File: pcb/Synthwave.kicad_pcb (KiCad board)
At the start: 2 copper layers, 68.8 x 136.6 mm, 62 parts, among them J1 Conn_01x01_Pin, J2 Conn_01x01_Pin, P1 MINI-360, P2 MINI-360, Q1 TIP120, Q10 TIP120, Q2 TIP120, Q3 TIP120, Q4 TIP120, Q5 TIP120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

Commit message: Many small updates
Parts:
- added J3: ADC1, Connector_PinSocket_2.54mm:PinSocket_1x03_P2.54mm_Vertical, F.Cu at (66.0, 16.5)
- added J4: ADC2, Connector_PinSocket_2.54mm:PinSocket_1x03_P2.54mm_Vertical, F.Cu at (67.0, 45.7)
- added J5: ADC3, Connector_PinSocket_2.54mm:PinSocket_1x03_P2.54mm_Vertical, F.Cu at (71.6, 45.7)
- added J6: ADC4, Connector_PinSocket_2.54mm:PinSocket_1x03_P2.54mm_Vertical, F.Cu at (76.2, 45.7)
- U1: value Heltec_HTIT-WB32 -> Heltec_HTIT-WB32v3
- moved U2 8.84 mm to (52.1, 52.4)
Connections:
- P2 pad 2: Net-(P2-OUT-) -> Net-(J3-PIN_3)
- P2 pad 3: Net-(P2-OUT+) -> Net-(J3-Pin_2)
- R1 pad 2: Net-(R1-Pad2) -> Net-(U1-7_ADC)
- R10 pad 2: Net-(R10-Pad2) -> Net-(U1-42)
- R11 pad 1: Net-(R1-Pad2) -> Net-(U1-7_ADC)
- R12 pad 1: Net-(R12-Pad1) -> Net-(U1-6_ADC)
- R13 pad 1: Net-(U1-25_DAC) -> Net-(U1-33)
- R14 pad 1: Net-(R14-Pad1) -> Net-(U1-47)
- R15 pad 1: Net-(R15-Pad1) -> Net-(U1-48)
- R16 pad 1: Net-(R16-Pad1) -> Net-(U1-46)
- R17 pad 1: Net-(R17-Pad1) -> Net-(U1-5_ADC)
- R18 pad 1: Net-(R18-Pad1) -> Net-(U1-34)
- R19 pad 1: Net-(R19-Pad1) -> Net-(U1-45)
- R2 pad 2: Net-(R12-Pad1) -> Net-(U1-6_ADC)
- R20 pad 1: Net-(R10-Pad2) -> Net-(U1-42)
- R3 pad 2: Net-(U1-25_DAC) -> Net-(U1-33)
- R4 pad 2: Net-(R14-Pad1) -> Net-(U1-47)
- R5 pad 2: Net-(R15-Pad1) -> Net-(U1-48)
- R6 pad 2: Net-(R16-Pad1) -> Net-(U1-46)
- R7 pad 2: Net-(R17-Pad1) -> Net-(U1-5_ADC)
- R8 pad 2: Net-(R18-Pad1) -> Net-(U1-34)
- R9 pad 2: Net-(R19-Pad1) -> Net-(U1-45)
- U1 pad 1: unconnected-(U1-TX-Pad1) -> Net-(U1-48)
- U1 pad 12: Net-(R18-Pad1) -> unconnected-(U1-43_TX-Pad12)
- U1 pad 13: Net-(R17-Pad1) -> unconnected-(U1-44_RX-Pad13)
- U1 pad 14: Net-(R1-Pad2) -> unconnected-(U1-RST-Pad14)
- U1 pad 15: unconnected-(U1-15_OLED-Pad15) -> Net-(U1-33)
- U1 pad 17: Net-(R16-Pad1) -> unconnected-(U1-38-Pad17)
- U1 pad 18: unconnected-(U1-Pad18) -> Net-(U1-40)
- U1 pad 19: unconnected-(U1-Pad19) -> Net-(U1-42)
- U1 pad 2: Net-(R19-Pad1) -> Net-(U1-34)
- U1 pad 20: Net-(P2-OUT+) -> unconnected-(U1-3.3V-Pad20)
- U1 pad 21: unconnected-(U1-Pad21) -> Net-(U1-46)
- U1 pad 22: unconnected-(U1-Pad22) -> Net-(U1-45)
- U1 pad 23: Net-(R10-Pad2) -> Net-(U1-41)
- U1 pad 25: Net-(U1-25_DAC) -> unconnected-(U1-20-Pad25)
- U1 pad 27: Net-(R12-Pad1) -> unconnected-(U1-USER_SW_0-Pad27)
- U1 pad 28: Net-(P2-OUT-) -> unconnected-(U1-GND-Pad28)
- U1 pad 3: unconnected-(U1-RX-Pad3) -> Net-(U1-47)
- U1 pad 32: Net-(R15-Pad1) -> Net-(U1-7_ADC)
- U1 pad 33: Net-(R14-Pad1) -> unconnected-(U1-19_CLK-Pad33)
- U1 pad 34: Net-(U2-IB) -> Net-(U1-5_ADC)
- U1 pad 35: Net-(U2-IA) -> Net-(U1-6_ADC)
- U1 pad 36: unconnected-(U1-Pad36) -> Net-(J3-Pin_1)
- U1 pad 37: unconnected-(U1-Pad37) -> Net-(J4-Pin_1)
- U1 pad 38: unconnected-(U1-Pad38) -> Net-(J5-Pin_1)
- U1 pad 39: unconnected-(U1-Pad39) -> Net-(J6-Pin_1)
- U1 pad 8: unconnected-(U1-GND-Pad8) -> Net-(J3-PIN_3)
- U1 pad 9: unconnected-(U1-3.3-Pad9) -> Net-(J3-Pin_2)
- U2 pad 5: Net-(P2-OUT-) -> Net-(J3-PIN_3)
- U2 pad 6: Net-(U2-IA) -> Net-(U1-40)
- U2 pad 7: Net-(U2-IB) -> Net-(U1-41)
- U2 pad 8: Net-(P2-OUT-) -> Net-(J3-PIN_3)
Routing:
- net GND: track 300.9 -> 0.00 mm
- net +15V: track 266.4 -> 0.00 mm
- net Net-(R1-Pad2): track 112.5 -> 0.00 mm
- net Net-(P2-OUT-): track 93.5 -> 0.00 mm
- net Net-(R12-Pad1): track 91.5 -> 0.00 mm, vias 1 -> 0
- net Net-(U1-25_DAC): track 89.5 -> 0.00 mm
- net Net-(R14-Pad1): track 81.5 -> 0.00 mm
- net Net-(P2-OUT+): track 68.1 -> 0.00 mm
- net Net-(R10-Pad2): track 67.1 -> 0.00 mm
- net Net-(R17-Pad1): track 63.9 -> 0.00 mm
- net Net-(U2-IB): track 54.5 -> 0.00 mm
- net Net-(U2-IA): track 53.3 -> 0.00 mm
- net Net-(R18-Pad1): track 52.3 -> 0.00 mm
- net Net-(R15-Pad1): track 48.8 -> 0.00 mm
- net Net-(E2-Pin_1): track 42.0 -> 0.00 mm
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
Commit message: Update and upgrades
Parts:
- removed DC_OUT1, DC_OUT10, DC_OUT2, DC_OUT3, DC_OUT4, DC_OUT5, DC_OUT6, DC_OUT7, DC_OUT8, DC_OUT9: GND, Connector_PinSocket_2.54mm:PinSocket_1x02_P2.54mm_Vertical
- removed the G*** at (65.1, 136.6)
- added G***: LOGO, Untitled, F.Cu at (58.4, 118.1)
- added J7: RX, Connector_PinSocket_2.54mm:PinSocket_1x02_P2.54mm_Vertical, F.Cu at (67.3, 58.4)
- added J8: RX, Connector_PinSocket_2.54mm:PinSocket_1x02_P2.54mm_Vertical, F.Cu at (71.1, 58.4)
- added PUMP1: GND, Connector_PinSocket_2.54mm:PinSocket_1x02_P2.54mm_Vertical, F.Cu at (20.3, 26.7)
- added PUMP2: GND, Connector_PinSocket_2.54mm:PinSocket_1x02_P2.54mm_Vertical, F.Cu at (20.3, 35.6)
- added REL1: GND, Connector_PinSocket_2.54mm:PinSocket_1x02_P2.54mm_Vertical, F.Cu at (20.3, 102.9)
- added REL2: GND, Connector_PinSocket_2.54mm:PinSocket_1x02_P2.54mm_Vertical, F.Cu at (20.3, 110.5)
- added VAC1: GND, Connector_PinSocket_2.54mm:PinSocket_1x02_P2.54mm_Vertical, F.Cu at (20.3, 83.8)
- added VAC2: GND, Connector_PinSocket_2.54mm:PinSocket_1x02_P2.54mm_Vertical, F.Cu at (20.3, 94.0)
- added VALVE1: GND, Connector_PinSocket_2.54mm:PinSocket_1x02_P2.54mm_Vertical, F.Cu at (20.3, 44.5)
- added VALVE2: GND, Connector_PinSocket_2.54mm:PinSocket_1x02_P2.54mm_Vertical, F.Cu at (20.3, 53.3)
- added VALVE3: GND, Connector_PinSocket_2.54mm:PinSocket_1x02_P2.54mm_Vertical, F.Cu at (20.3, 62.2)
- added VALVE4: GND, Connector_PinSocket_2.54mm:PinSocket_1x02_P2.54mm_Vertical, F.Cu at (20.3, 72.4)
- moved H3 28.1 mm to (71.1, 119.4)
- moved H2 27.1 mm to (19.1, 119.4)
- moved D10 26.1 mm to (24.1, 119.6)
- moved R10 25.2 mm to (36.9, 114.3)
- moved R20 25.2 mm to (36.9, 119.4)
- moved Q10 25.2 mm to (26.6, 115.5)
- moved U2 22.2 mm to (55.9, 30.5)
- moved D9 22.1 mm to (24.0, 109.5)
- moved R19 20.9 mm to (36.8, 109.5)
- moved R9 20.9 mm to (36.8, 104.4)
- moved Q9 20.9 mm to (26.5, 105.5)
- moved J3 19.1 mm to (67.3, 35.6)
- moved D8 18.5 mm to (24.0, 99.3)
- moved R8 17.4 mm to (36.8, 94.2)
- moved R18 17.4 mm to (36.8, 99.3)
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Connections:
- U1 pad 12: unconnected-(U1-43_TX-Pad12) -> Net-(J7-Pin_1)
- U1 pad 13: unconnected-(U1-44_RX-Pad13) -> Net-(J7-Pin_2)
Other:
- board size 68.8 x 136.6 mm -> 57.1 x 102.9 mm

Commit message: updates
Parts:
- removed J2: Conn_01x01_Pin, Connector_PinSocket_2.54mm:PinSocket_1x01_P2.54mm_Vertical
- removed P2: MINI-360, Custom Footprints:MINI-360
- added J10: GPIO39, Connector_PinSocket_2.54mm:PinSocket_1x02_P2.54mm_Vertical, F.Cu at (61.0, 54.6)
- added J9: GPIO26, Connector_PinSocket_2.54mm:PinSocket_1x02_P2.54mm_Vertical, F.Cu at (56.9, 54.6)
- added NT1: NetTie_2, NetTie:NetTie-2_THT_Pad1.0mm, F.Cu at (62.7, 34.3)
- added U3: L7805, Package_TO_SOT_THT:TO-220-3_Vertical, F.Cu at (52.1, 58.4)
- J1: value Conn_01x01_Pin -> Barrel_Jack_Switch; footprint Connector_PinSocket_2.54mm:PinSocket_1x01_P2.54mm_Vertical -> Connector_BarrelJack:BarrelJack_Horizontal
- J7: value RX -> TX
- moved U2 10.9 mm to (66.8, 29.7), turned to 180 degrees
- moved J1 6.96 mm to (52.6, 32.9), turned to -90 degrees
- moved P1 2.54 mm to (55.9, 41.8)
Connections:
- net Net-(J3-Pin_2) renamed +5V
- J3 pad 3: Net-(J3-PIN_3) -> GND1
- J4 pad 3: Net-(J3-PIN_3) -> GND1
- J5 pad 3: Net-(J3-PIN_3) -> GND1
- J6 pad 3: Net-(J3-PIN_3) -> GND1
- J8 pad 1: Net-(J3-PIN_3) -> GND1
- R11 pad 2: GND -> GND1
- R12 pad 2: GND -> GND1
- R13 pad 2: GND -> GND1
- R14 pad 2: GND -> GND1
- R15 pad 2: GND -> GND1
- R16 pad 2: GND -> GND1
- R17 pad 2: GND -> GND1
- R18 pad 2: GND -> GND1
- R19 pad 2: GND -> GND1
- R20 pad 2: GND -> GND1
- U1 pad 10: unconnected-(U1-26-Pad10) -> Net-(J9-Pin_1)
- U1 pad 5: unconnected-(U1-39-Pad5) -> Net-(J10-Pin_1)
- U1 pad 8: Net-(J3-PIN_3) -> GND1
- U2 pad 5: Net-(J3-PIN_3) -> GND
- U2 pad 8: Net-(J3-PIN_3) -> GND
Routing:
- net +15V: track 0.00 -> 218.0 mm
- net GND1: track 0.00 -> 200.9 mm
- net GND: track 0.00 -> 146.8 mm
- net +5V: track 0.00 -> 128.7 mm
- net Net-(U1-7_ADC): track 0.00 -> 77.7 mm
- net Net-(U1-40): track 0.00 -> 75.2 mm
- net Net-(U1-6_ADC): track 0.00 -> 68.2 mm, vias 0 -> 1
- net Net-(U1-5_ADC): track 0.00 -> 63.2 mm, vias 0 -> 2
- net Net-(U1-33): track 0.00 -> 61.2 mm
- net Net-(U1-48): track 0.00 -> 55.6 mm
- net Net-(U1-47): track 0.00 -> 53.8 mm
- net Net-(U1-42): track 0.00 -> 53.2 mm
- net Net-(U1-41): track 0.00 -> 52.3 mm
- net Net-(J9-Pin_1): track 0.00 -> 51.8 mm, vias 0 -> 1
- net Net-(U1-45): track 0.00 -> 45.8 mm
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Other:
- board text added: "RX"
- board text added: "TX"

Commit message: Add model updates and various files
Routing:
- net Net-(U1-5_ADC): track 63.2 -> 115.2 mm, vias 2 -> 0
- net +15V: track 218.0 -> 191.9 mm
- net Net-(U1-7_ADC): track 77.7 -> 96.6 mm
- net Net-(U1-40): track 75.2 -> 57.4 mm
- net +5V: track 128.7 -> 115.7 mm
- net Net-(D9-A): track 32.8 -> 21.5 mm
- net Net-(U1-48): track 55.6 -> 46.2 mm
- net Net-(U1-45): track 45.8 -> 55.1 mm
- net Net-(U1-41): track 52.3 -> 61.6 mm
- net Net-(Q6-B): track 11.1 -> 19.4 mm
- net Net-(Q9-B): track 11.1 -> 19.4 mm
- net Net-(U1-34): track 16.9 -> 24.6 mm
- net GND1: track 200.9 -> 206.0 mm
- net Net-(D6-A): track 25.5 -> 21.7 mm
- net GND: track 146.8 -> 143.5 mm
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
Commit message: Update electrode information, many small tweaks
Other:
- board text removed: "RX"
- board text removed: "TX"
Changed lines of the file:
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@@
         (effects (font (size 1 1) (thickness 0.15)))
     )
-    (fp_text value "RX" (at 0 5.31) (layer "F.Fab")
+    (fp_text value "RX" (at 0 5.31) (layer "F.Fab") hide
         (effects (font (size 1 1) (thickness 0.15)))
     )
@@
         (effects (font (size 1 1) (thickness 0.15)))
     )
-    (fp_text value "TX" (at 0 5.31) (layer "F.Fab")
+    (fp_text value "TX" (at 0 5.31) (layer "F.Fab") hide
         (effects (font (size 1 1) (thickness 0.15)))
     )
@@
     (effects (font (size 1 1) (thickness 0.15)))
   )
-  (gr_text "RX" (at 70.104 64.262) (layer "F.SilkS")
-    (effects (font (size 1 1) (thickness 0.15)) (justify left bottom))
-  )
-  (gr_text "TX" (at 66.294 64.262) (layer "F.SilkS")
-    (effects (font (size 1 1) (thickness 0.15)) (justify left bottom))
-  )
   (gr_text "GND" (at 52.578 24.384) (layer "F.SilkS")

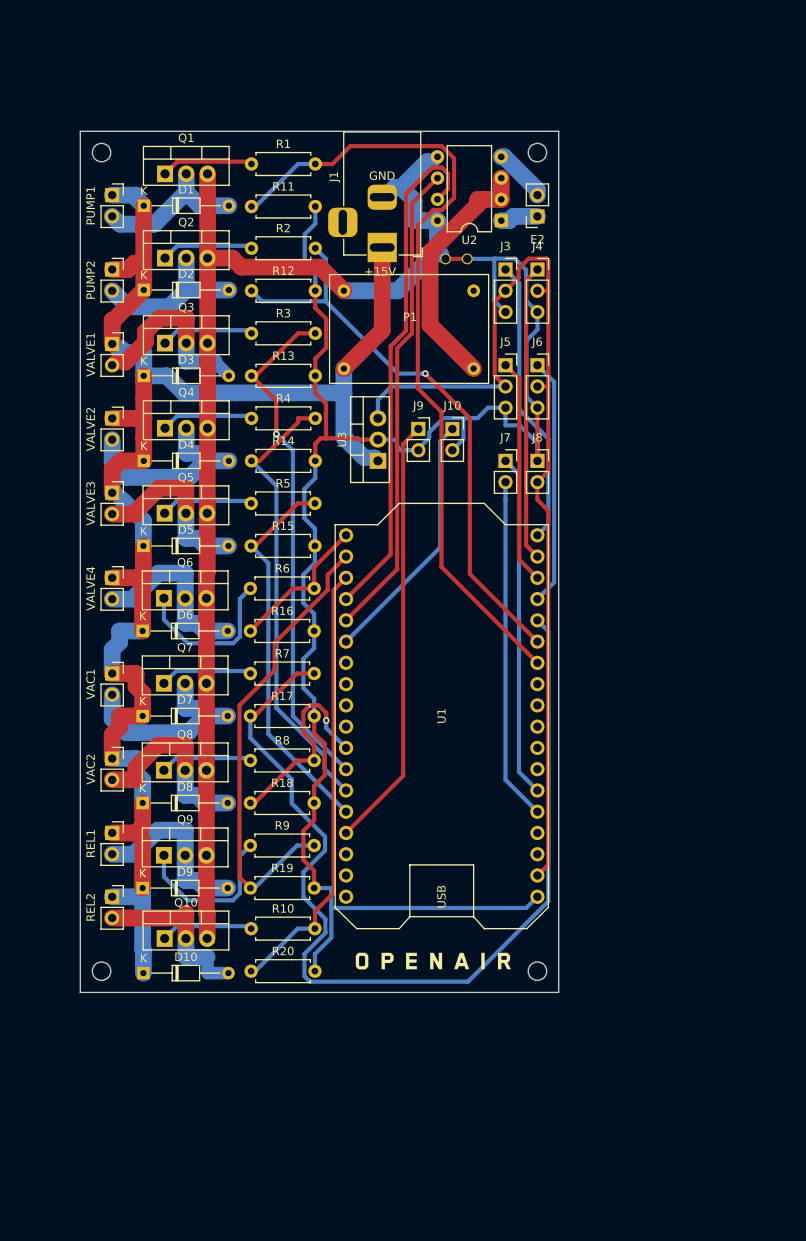
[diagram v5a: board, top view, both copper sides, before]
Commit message: Add lots and lots of connectors to PCB
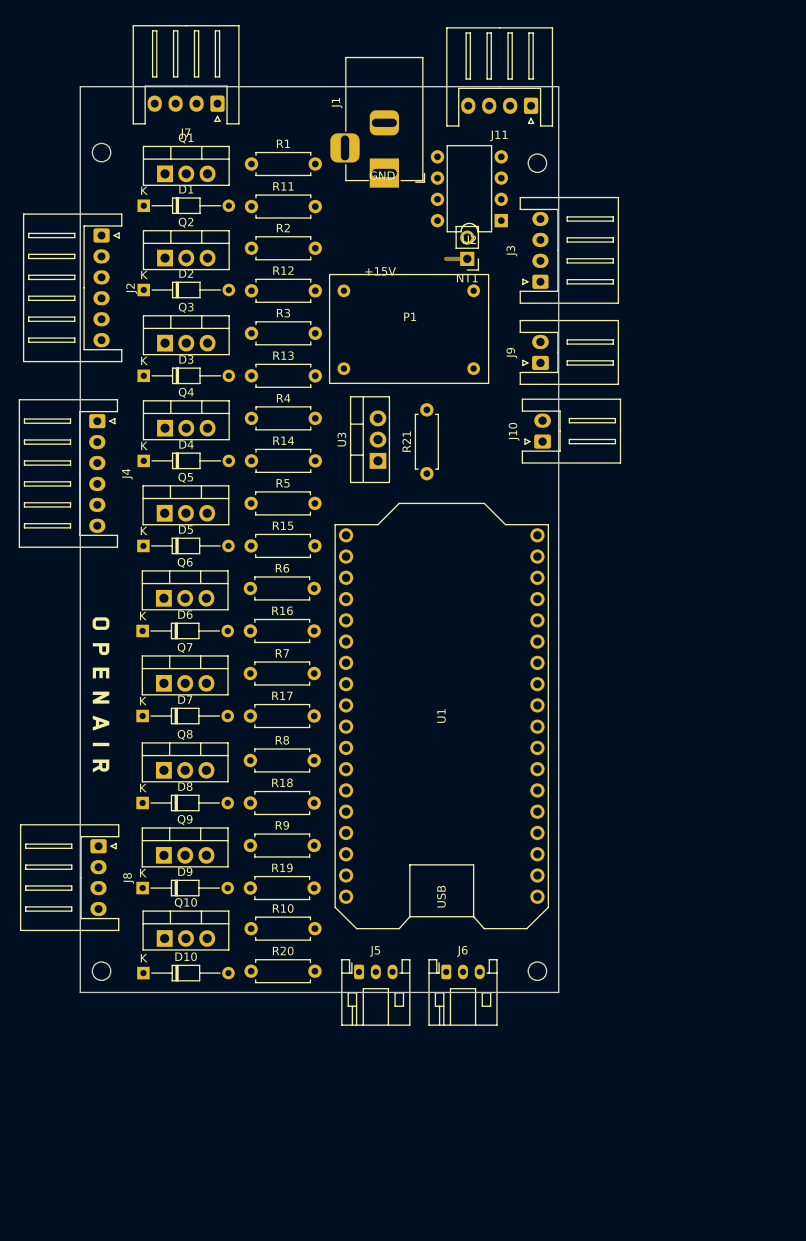
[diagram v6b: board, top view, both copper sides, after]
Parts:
- removed E2: E1, Connector_PinSocket_2.54mm:PinSocket_1x02_P2.54mm_Vertical
- removed PUMP1, PUMP2, REL1, REL2, VAC1, VAC2, VALVE1, VALVE2, VALVE3, VALVE4: GND, Connector_PinSocket_2.54mm:PinSocket_1x02_P2.54mm_Vertical
- added J11: Conn_01x04_Socket, Connector_JST:JST_XH_S4B-XH-A_1x04_P2.50mm_Horizontal, F.Cu at (70.4, 16.0)
- added J2: Conn_01x06_Socket, Connector_JST:JST_XH_S6B-XH-A_1x06_P2.50mm_Horizontal, F.Cu at (19.1, 31.5)
- added R21: 1k, Resistor_THT:R_Axial_DIN0207_L6.3mm_D2.5mm_P7.62mm_Horizontal, F.Cu at (57.9, 59.9)
- J10, J9: footprint Connector_PinSocket_2.54mm:PinSocket_1x02_P2.54mm_Vertical -> Connector_JST:JST_XH_S2B-XH-A_1x02_P2.50mm_Horizontal
- J3: value ADC1 -> SDA; footprint Connector_PinSocket_2.54mm:PinSocket_1x03_P2.54mm_Vertical -> Connector_JST:JST_XH_S4B-XH-A_1x04_P2.50mm_Horizontal
- J4: value ADC2 -> Conn_01x06_Socket; footprint Connector_PinSocket_2.54mm:PinSocket_1x03_P2.54mm_Vertical -> Connector_JST:JST_XH_S6B-XH-A_1x06_P2.50mm_Horizontal
- J5, J6: footprint Connector_PinSocket_2.54mm:PinSocket_1x03_P2.54mm_Vertical -> Connector_JST:JST_PH_S3B-PH-K_1x03_P2.00mm_Horizontal
- J7: value TX -> Conn_01x04_Socket; footprint Connector_PinSocket_2.54mm:PinSocket_1x02_P2.54mm_Vertical -> Connector_JST:JST_XH_S4B-XH-A_1x04_P2.50mm_Horizontal
- J8: value RX -> Conn_01x04_Socket; footprint Connector_PinSocket_2.54mm:PinSocket_1x02_P2.54mm_Vertical -> Connector_JST:JST_XH_S4B-XH-A_1x04_P2.50mm_Horizontal
- NT1: footprint NetTie:NetTie-2_THT_Pad1.0mm -> Connector_PinHeader_2.54mm:PinHeader_1x02_P2.54mm_Vertical
- moved J5 74.6 mm to (49.8, 119.5)
- moved J6 73.3 mm to (60.2, 119.5)
- moved J8 69.8 mm to (18.7, 104.5), turned to -90 degrees
- moved J4 55.6 mm to (18.5, 53.7), turned to -90 degrees
- moved J7 54.8 mm to (32.9, 15.7), turned to 180 degrees
- moved G*** 50.7 mm to (19.1, 86.1), turned to -90 degrees
- moved J9 16.6 mm to (71.5, 46.7), turned to 90 degrees
- moved J10 10.9 mm to (71.7, 56.1), turned to 90 degrees
- moved J1 8.89 mm to (52.8, 24.0)
- moved J3 4.42 mm to (71.5, 37.0), turned to 90 degrees
- moved H4 1.27 mm to (71.1, 22.9)
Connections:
- J3 pad 2: +5V -> Net-(J3-Pin_2)
- J3 pad 3: GND1 -> Net-(J3-Pin_3)
- J4 pad 1: Net-(J4-Pin_1) -> Net-(D6-A)
- J4 pad 2: +5V -> +15V
- J4 pad 3: GND1 -> Net-(D5-A)
- J7 pad 1: Net-(J7-Pin_1) -> Net-(D8-A)
- J7 pad 2: Net-(J7-Pin_2) -> +15V
- J8 pad 1: GND1 -> Net-(D10-A)
- J8 pad 2: +5V -> +15V
- U1 pad 10: Net-(J9-Pin_1) -> unconnected-(U1-26-Pad10)
- U1 pad 11: unconnected-(U1-3.3V-Pad11) -> Net-(J3-Pin_3)
- U1 pad 12: Net-(J7-Pin_1) -> unconnected-(U1-43_TX-Pad12)
- U1 pad 13: Net-(J7-Pin_2) -> unconnected-(U1-44_RX-Pad13)
- U1 pad 25: unconnected-(U1-20-Pad25) -> Net-(J9-Pin_1)
- U1 pad 37: Net-(J4-Pin_1) -> Net-(J3-Pin_2)
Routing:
- net GND1: track 206.0 -> 0.00 mm
- net +15V: track 191.9 -> 0.00 mm
- net GND: track 143.5 -> 0.00 mm
- net +5V: track 115.7 -> 0.00 mm
- net Net-(U1-5_ADC): track 115.2 -> 0.00 mm
- net Net-(U1-7_ADC): track 96.6 -> 0.00 mm
- net Net-(U1-6_ADC): track 69.3 -> 0.00 mm, vias 1 -> 0
- net Net-(U1-41): track 61.6 -> 0.00 mm
- net Net-(U1-33): track 61.3 -> 0.00 mm, vias 1 -> 0
- net Net-(U1-40): track 57.4 -> 0.00 mm
- net Net-(U1-45): track 55.1 -> 0.00 mm
- net Net-(U1-47): track 54.0 -> 0.00 mm
- net Net-(U1-42): track 53.2 -> 0.00 mm
- net Net-(J9-Pin_1): track 51.8 -> 0.00 mm
- net Net-(U1-48): track 46.2 -> 0.00 mm
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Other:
- board size 57.1 x 102.9 mm -> 57.1 x 108.2 mm

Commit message: Switch to better buck converter board
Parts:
- removed P1: MINI-360, Custom Footprints:MINI-360
- added U4: XL4015-5A-PS, Custom Footprints:XL4015-5A-PS, F.Cu at (47.3, 65.0)
- J10 FLOAT2: renamed from J10
- J11 ELECTRODES: renamed from J11
- J2 PUMP1 VALVE1 VALVE4: renamed from J2
- J3 CO2 SENSOR: renamed from J3
- J4 PUMP2 VALVE2 VALVE3: renamed from J4
- J5 PH2: renamed from J5
- J6 PH1: renamed from J6
- J7 VAC1 VAC2: renamed from J7
- J8 REL1 REL2: renamed from J8
- J9 FLOAT2: renamed from J9
- moved J1 74.1 mm to (78.6, 93.5), turned to 180 degrees
- moved J4 PUMP2 VALVE2 VALVE3 62.3 mm to (79.5, 40.7), turned to 90 degrees
- moved J8 REL1 REL2 61.1 mm to (77.3, 121.7), turned to 0 degrees
- moved U2 54.1 mm to (82.5, 81.5)
- moved J9 FLOAT2 53.7 mm to (18.5, 55.6), turned to -90 degrees
- moved NT1 50.1 mm to (86.9, 78.2)
- moved J6 PH1 47.7 mm to (19.1, 95.3), turned to -90 degrees
- moved J5 PH2 38.3 mm to (86.4, 107.9), turned to 90 degrees
- moved J3 CO2 SENSOR 35.6 mm to (43.7, 14.7), turned to 180 degrees
- moved H4 29.6 mm to (100.1, 16.8)
- moved U3 28.2 mm to (79.5, 65.0)
- moved R21 28.0 mm to (85.1, 66.8)
- moved H3 23.4 mm to (94.0, 114.6)
- moved J11 ELECTRODES 16.7 mm to (87.1, 15.6)
- moved J10 FLOAT2 8.86 mm to (79.6, 52.0)
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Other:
- board size 57.1 x 108.2 mm -> 72.4 x 112.8 mm
